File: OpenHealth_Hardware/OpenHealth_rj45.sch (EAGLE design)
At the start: 7 parts

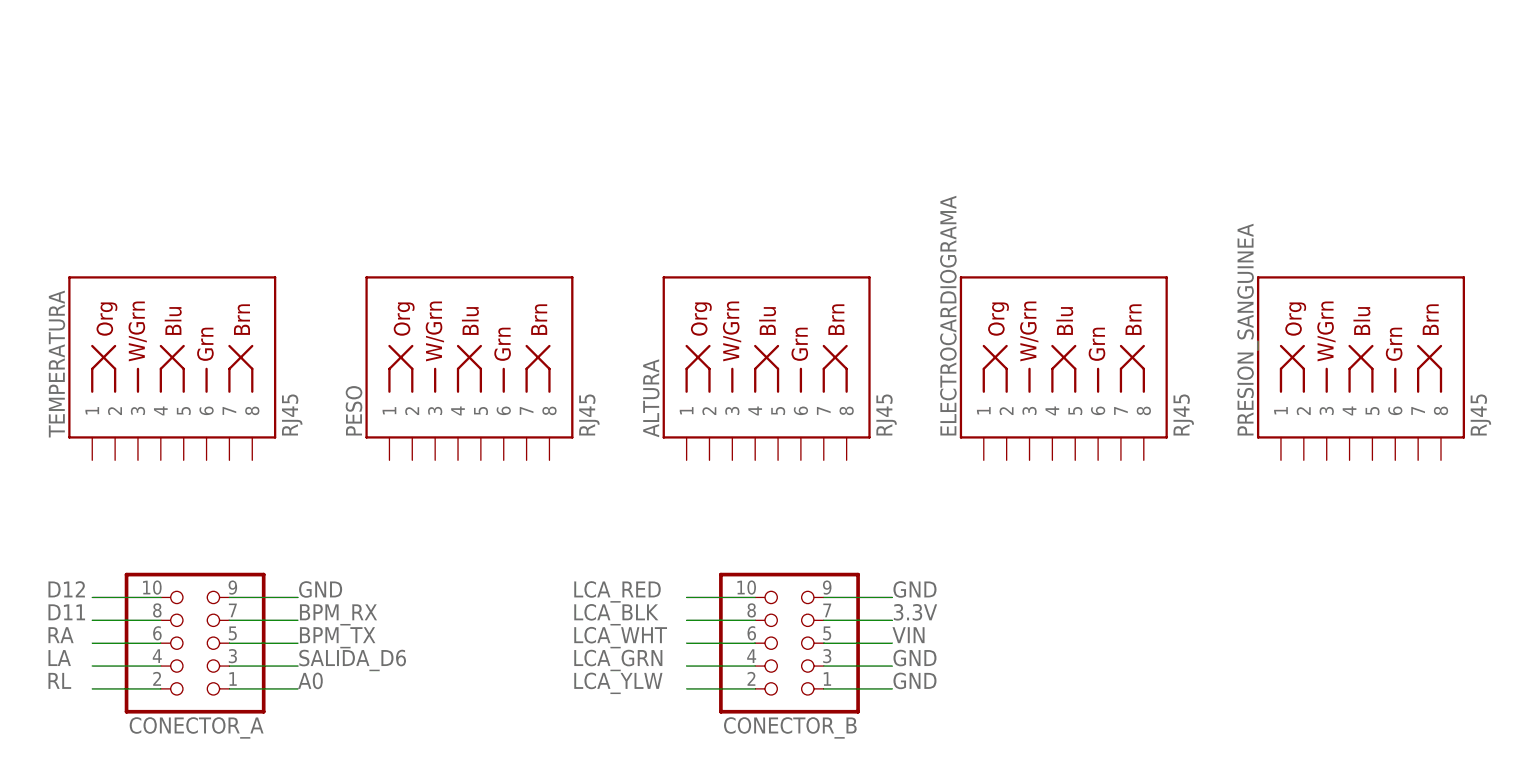
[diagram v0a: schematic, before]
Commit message: Eliminacion de archivos de cache, enrutado logico de las salidas del rj45, modificacion del archivo planteando mejoras
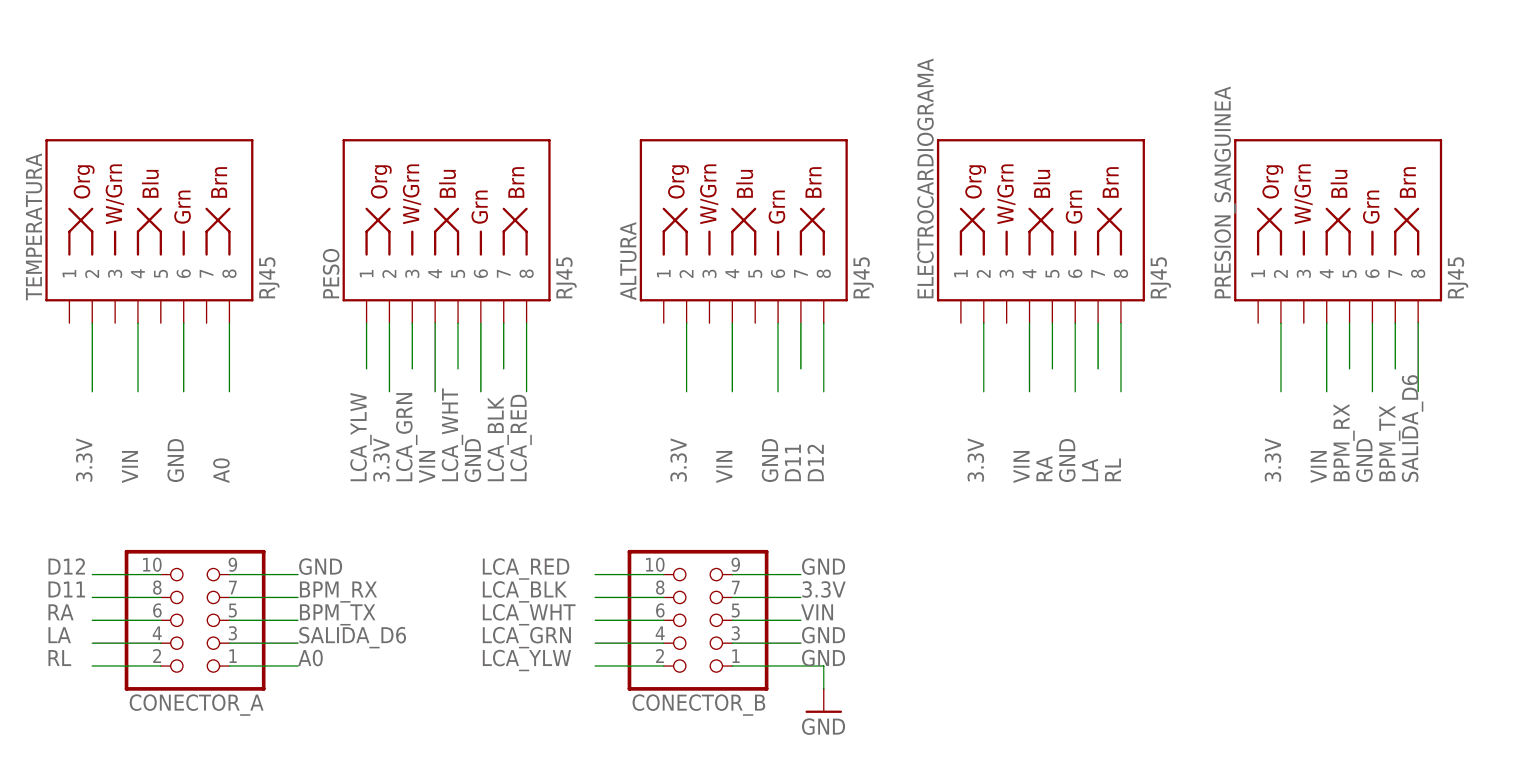
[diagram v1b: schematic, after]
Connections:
- net 3.3V: now also ALTURA.2, ELECTROCARDIOGRAMA.2, PESO.2, PRESION_SANGUINEA.2, TEMPERATURA.2
- net A0: now also TEMPERATURA.8
- net BPM_RX: now also PRESION_SANGUINEA.5
- net BPM_TX: now also PRESION_SANGUINEA.7
- net D11: now also ALTURA.7
- net D12: now also ALTURA.8
- net GND: now also ALTURA.6, ELECTROCARDIOGRAMA.6, PESO.6, PRESION_SANGUINEA.6, TEMPERATURA.6
- net LA: now also ELECTROCARDIOGRAMA.7
- net LCA_BLK: now also PESO.7
- net LCA_GRN: now also PESO.3
- net LCA_RED: now also PESO.8
- net LCA_WHT: now also PESO.5
- net LCA_YLW: now also PESO.1
- net RA: now also ELECTROCARDIOGRAMA.5
- net RL: now also ELECTROCARDIOGRAMA.8
- net SALIDA_D6: now also PRESION_SANGUINEA.8
- net VIN: now also ALTURA.4, ELECTROCARDIOGRAMA.4, PESO.4, PRESION_SANGUINEA.4, TEMPERATURA.4
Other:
- moved on the sheet: ALTURA, CONECTOR_A, CONECTOR_B, ELECTROCARDIOGRAMA, PESO, PRESION_SANGUINEA, TEMPERATURA

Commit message: Enrutado del de la placa de los conectores del RJ45 y se comienzo del proceso de ordenamiento de la placa principal
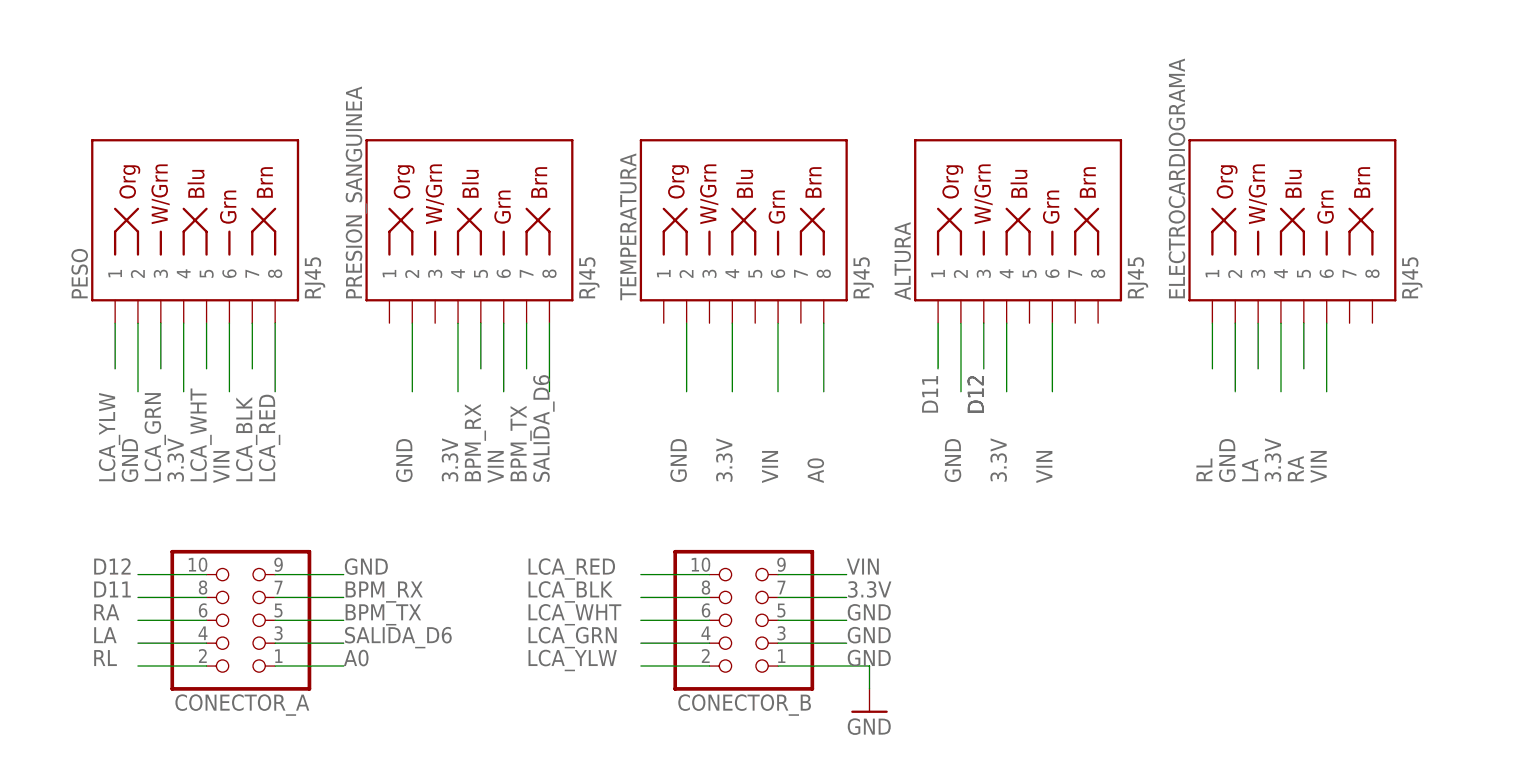
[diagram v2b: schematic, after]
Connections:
- net 3.3V: now also ALTURA.4, ELECTROCARDIOGRAMA.4, PESO.4, PRESION_SANGUINEA.4, TEMPERATURA.4; no longer ALTURA.2, ELECTROCARDIOGRAMA.2, PESO.2, PRESION_SANGUINEA.2, TEMPERATURA.2
- net D11: now also ALTURA.1; no longer ALTURA.7
- net D12: now also ALTURA.3; no longer ALTURA.8
- net GND: now also ALTURA.2, CONECTOR_B.5, ELECTROCARDIOGRAMA.2, PESO.2, PRESION_SANGUINEA.2, TEMPERATURA.2; no longer ALTURA.6, CONECTOR_B.9, ELECTROCARDIOGRAMA.6, PESO.6, PRESION_SANGUINEA.6, TEMPERATURA.6
- net LA: now also ELECTROCARDIOGRAMA.3; no longer ELECTROCARDIOGRAMA.7
- net RL: now also ELECTROCARDIOGRAMA.1; no longer ELECTROCARDIOGRAMA.8
- net VIN: now also ALTURA.6, CONECTOR_B.9, ELECTROCARDIOGRAMA.6, PESO.6, PRESION_SANGUINEA.6, TEMPERATURA.6; no longer ALTURA.4, CONECTOR_B.5, ELECTROCARDIOGRAMA.4, PESO.4, PRESION_SANGUINEA.4, TEMPERATURA.4
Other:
- moved on the sheet: ALTURA, CONECTOR_A, CONECTOR_B, ELECTROCARDIOGRAMA, PESO, PRESION_SANGUINEA, TEMPERATURA
